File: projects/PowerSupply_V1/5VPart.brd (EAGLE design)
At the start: 49.5 x 58.4 mm, 24 parts, among them IC1 LM2596T, IC2 LM2596T, X1 IN, X2 OUT

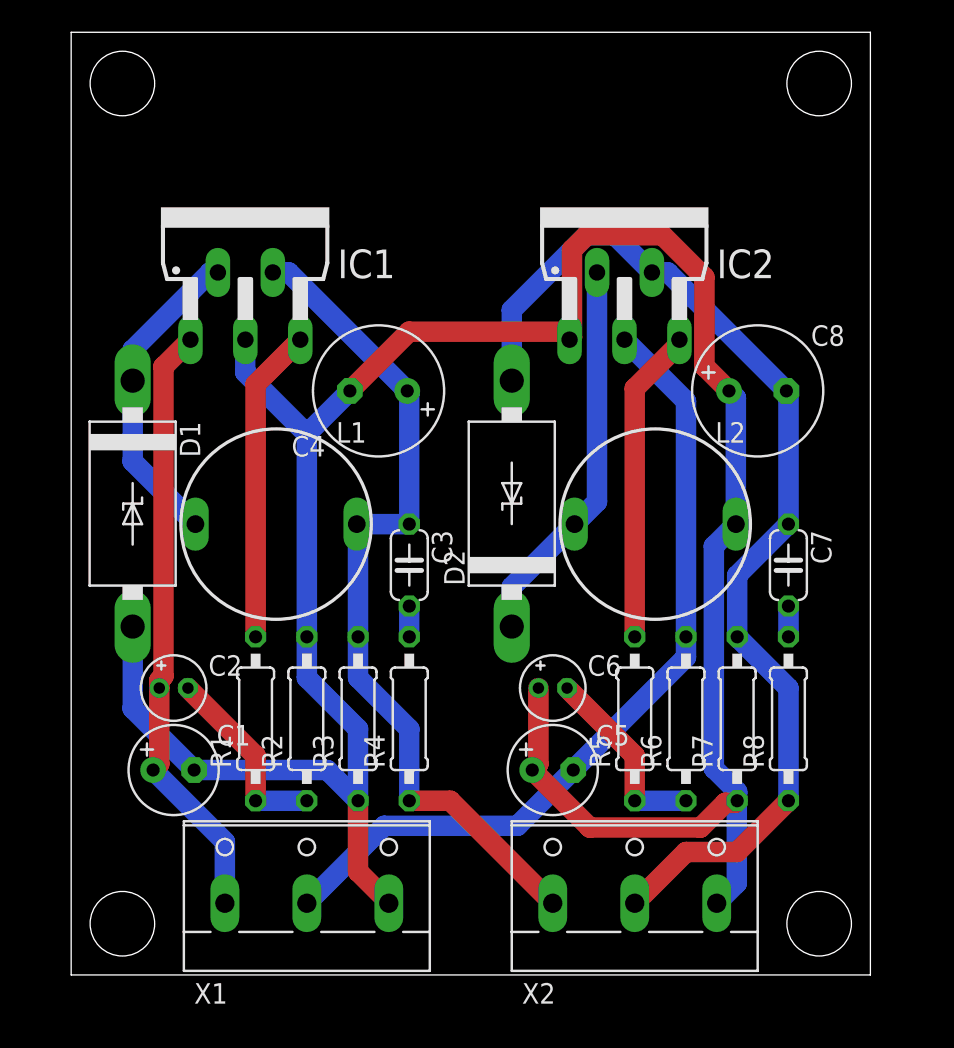
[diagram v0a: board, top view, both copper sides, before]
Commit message: refactor(5v): schematics changed
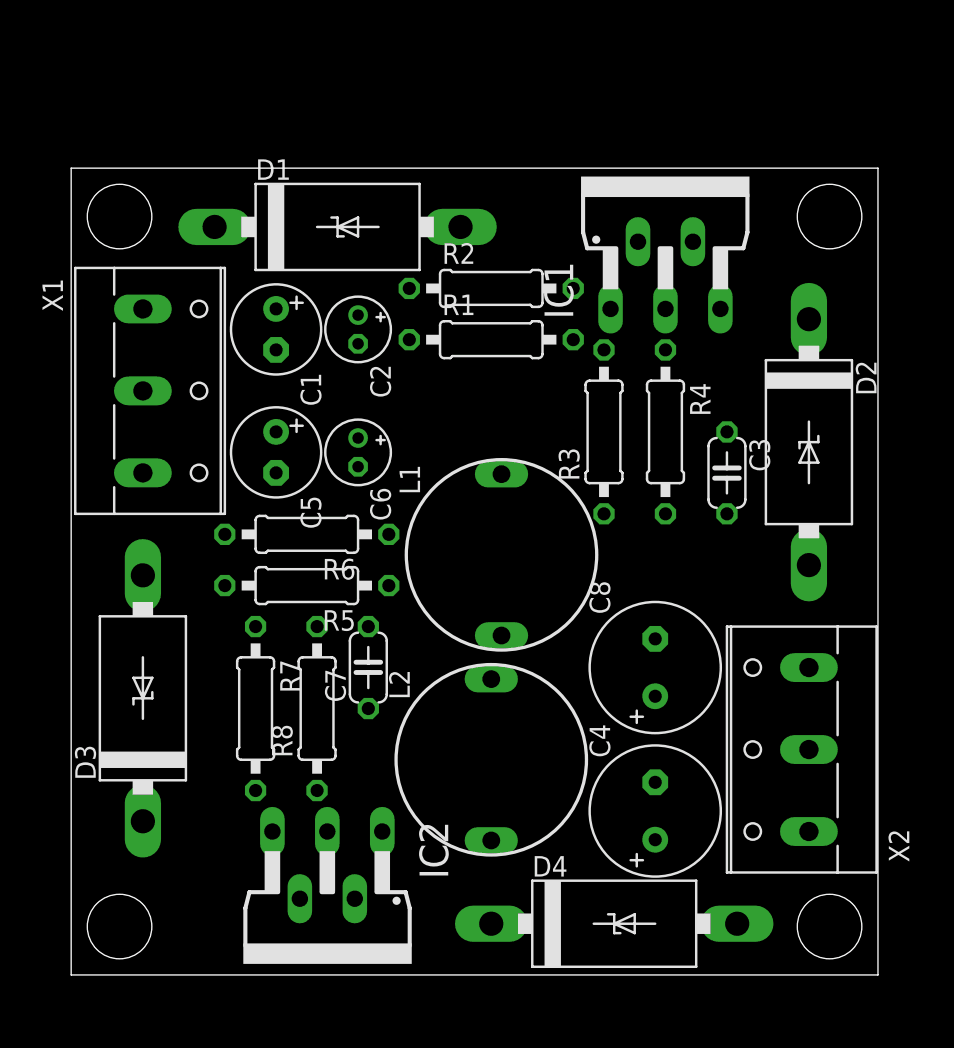
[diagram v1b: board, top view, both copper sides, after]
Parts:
- added D3, D4: 1N5822, diode:C4111-15
- moved IC2 44.6 mm to (15.9, 3.81), turned to 180 degrees
- moved X1 32.5 mm to (5.08, 36.2), turned to 270 degrees
- moved C4 31.2 mm to (36.2, 10.2), turned to 90 degrees
- moved R7 29.9 mm to (11.4, 16.5), turned to 270 degrees
- moved R8 29.2 mm to (15.2, 16.5)
- moved R2 29.0 mm to (26.0, 42.5), turned to 0 degrees
- moved C1 28.0 mm to (12.7, 40.0), turned to 270 degrees
- moved R1 27.7 mm to (26.0, 39.4), turned to 0 degrees
- moved C7 26.8 mm to (18.4, 19.1), turned to 90 degrees
- moved R6 26.1 mm to (14.6, 27.3), turned to 180 degrees
- moved C5 26.1 mm to (12.7, 32.4), turned to 270 degrees
- moved IC1 26.1 mm to (36.8, 46.4)
- moved C2 25.0 mm to (17.8, 40.0), turned to 270 degrees
- moved R4 23.8 mm to (36.8, 33.7), turned to 270 degrees
- moved R3 23.4 mm to (33.0, 33.7)
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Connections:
- net +24V: now also D1.C
- net -24V: now also D3.C, X1.3; no longer X1.2
- net -5V: now also D4.A, X2.3; no longer D2.A, X2.2
- net GND: now also D2.A, D3.A, X1.2, X2.2; no longer X1.3, X2.3
- net N$2: now also D4.C; no longer D2.C
- net N$3: now also D2.C; no longer D1.C
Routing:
- net GND: track 155.8 -> 0.00 mm
- net -5V: track 67.6 -> 0.00 mm
- net +5V: track 52.9 -> 0.00 mm
- net -24V: track 51.1 -> 0.00 mm
- net +24V: track 37.7 -> 0.00 mm
- net N$2: track 24.1 -> 0.00 mm
- net N$3: track 19.7 -> 0.00 mm
- net N$7: track 19.6 -> 0.00 mm
- net N$4: track 19.6 -> 0.00 mm
- net N$8: track 11.9 -> 0.00 mm
- net N$6: track 11.9 -> 0.00 mm
- net N$5: track 1.91 -> 0.00 mm
- net N$1: track 1.91 -> 0.00 mm
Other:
- board size 49.5 x 58.4 mm -> 50 x 50 mm

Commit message: refactor(5v): routing changed
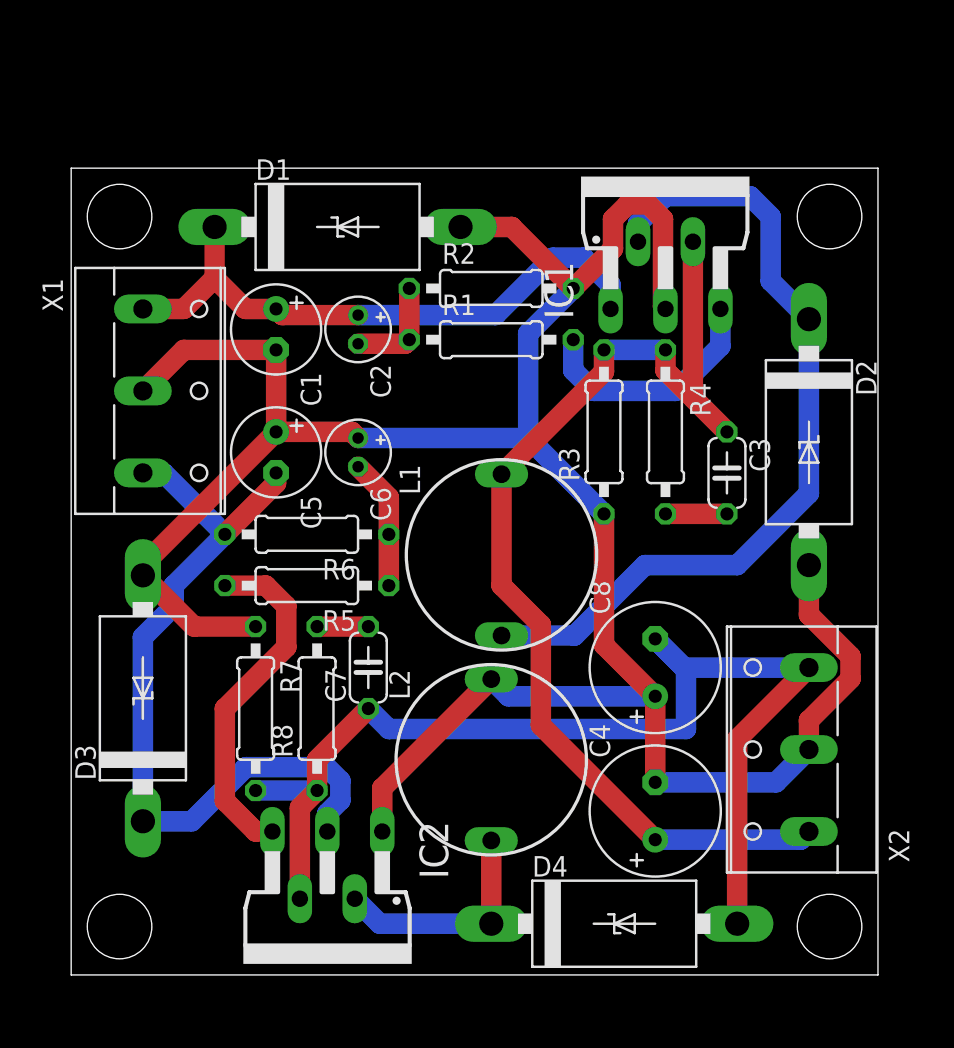
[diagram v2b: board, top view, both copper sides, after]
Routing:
- net GND: track 0.00 -> 155.9 mm
- net -5V: track 0.00 -> 71.9 mm
- net +5V: track 0.00 -> 69.8 mm
- net N$3: track 0.00 -> 51.4 mm
- net -24V: track 0.00 -> 49.1 mm
- net +24V: track 0.00 -> 38.2 mm
- net N$7: track 0.00 -> 21.7 mm
- net N$4: track 0.00 -> 15.0 mm
- net N$2: track 0.00 -> 14.3 mm
- net N$8: track 0.00 -> 8.16 mm
- net N$6: track 0.00 -> 6.46 mm
- net N$1: track 0.00 -> 3.81 mm
- net N$5: track 0.00 -> 3.17 mm

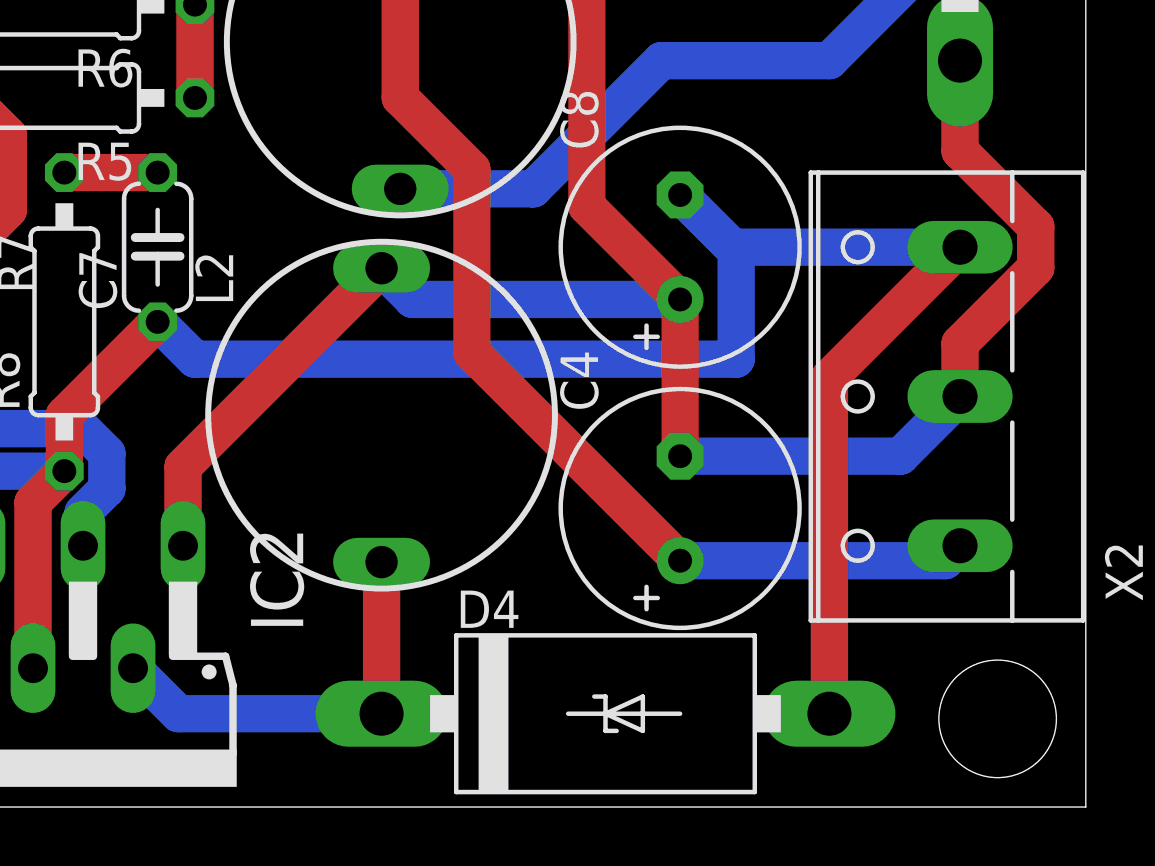
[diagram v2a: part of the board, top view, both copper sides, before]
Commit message: refactor(all): schematics and routing changed
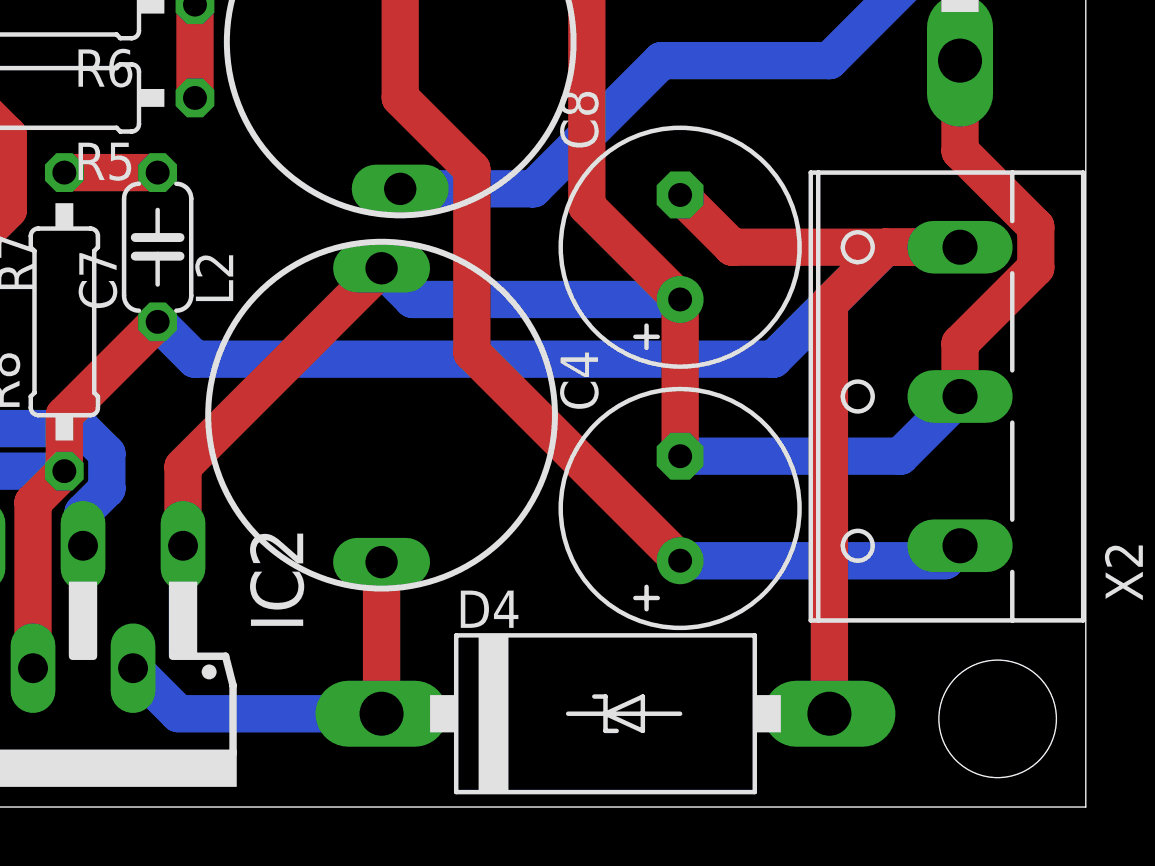
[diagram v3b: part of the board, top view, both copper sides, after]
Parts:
- C4: value 470µF -> 220µF
- C8: value 470µF -> 330µF
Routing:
- net -5V: track 71.9 -> 76.2 mm
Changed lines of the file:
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@@
 <attribute name="VALUE" x="37.973" y="33.274" size="1.27" layer="27" ratio="10" rot="R270"/>
 </element>
-<element name="C4" library="rcl" library_urn="urn:adsk.eagle:library:334" package="E3,5-8" package3d_urn="urn:adsk.eagle:package:23360/2" value="470µF" x="36.195" y="10.16" smashed="yes" rot="R90">
+<element name="C4" library="rcl" library_urn="urn:adsk.eagle:library:334" package="E3,5-8" package3d_urn="urn:adsk.eagle:package:23360/2" value="220µF" x="36.195" y="10.16" smashed="yes" rot="R90">
 <attribute name="NAME" x="33.401" y="13.462" size="1.27" layer="25" ratio="10" rot="R90"/>
 <attribute name="POPULARITY" value="13" x="66.675" y="29.21" size="1.778" layer="27" rot="R90" display="off"/>
@@
 <attribute name="VALUE" x="21.082" y="16.891" size="1.27" layer="27" ratio="10" rot="R90"/>
 </element>
-<element name="C8" library="rcl" library_urn="urn:adsk.eagle:library:334" package="E3,5-8" package3d_urn="urn:adsk.eagle:package:23360/2" value="470µF" x="36.195" y="19.05" smashed="yes" rot="R90">
+<element name="C8" library="rcl" library_urn="urn:adsk.eagle:library:334" package="E3,5-8" package3d_urn="urn:adsk.eagle:package:23360/2" value="330µF" x="36.195" y="19.05" smashed="yes" rot="R90">
 <attribute name="NAME" x="33.401" y="22.352" size="1.27" layer="25" ratio="10" rot="R90"/>
 <attribute name="POPULARITY" value="13" x="66.675" y="49.53" size="1.778" layer="27" rot="R90" display="off"/>
@@
 <wire x1="29.1074" y1="15.4696" x2="36.195" y2="8.382" width="1.27" layer="1"/>
 <wire x1="29.1074" y1="21.70288125" x2="29.1074" y2="15.4696" width="1.27" layer="1"/>
+<wire x1="33.02" y1="38.735" x2="36.83" y2="38.735" width="1.27" layer="16"/>
 <wire x1="36.195" y1="8.382" x2="45.212" y2="8.382" width="1.27" layer="16"/>
 <wire x1="45.212" y1="8.382" x2="45.72" y2="8.89" width="1.27" layer="16"/>
-<wire x1="33.02" y1="38.735" x2="36.83" y2="38.735" width="1.27" layer="16"/>
 </signal>
 <signal name="-5V">
+<contactref element="X2" pad="3"/>
 <contactref element="C8" pad="-"/>
 <contactref element="IC2" pad="4"/>
@@
 <contactref element="C7" pad="1"/>
 <contactref element="D4" pad="A"/>
-<contactref element="X2" pad="3"/>
 <wire x1="14.1732" y1="4.7244" x2="14.1732" y2="10.3632" width="1.27" layer="1"/>
 <wire x1="14.1732" y1="10.3632" x2="15.24" y2="11.43" width="1.27" layer="1"/>
 <wire x1="15.24" y1="11.43" x2="15.24" y2="13.335" width="1.27" layer="1"/>
 <wire x1="15.24" y1="13.335" x2="18.415" y2="16.51" width="1.27" layer="1"/>
-<wire x1="41.275" y1="3.175" x2="41.275" y2="14.605" width="1.27" layer="1"/>
-<wire x1="41.275" y1="14.605" x2="45.72" y2="19.05" width="1.27" layer="1"/>
 <wire x1="11.43" y1="11.43" x2="15.24" y2="11.43" width="1.27" layer="16"/>
-<wire x1="45.72" y1="19.05" x2="37.973" y2="19.05" width="1.27" layer="16"/>
-<wire x1="37.973" y1="19.05" x2="36.195" y2="20.828" width="1.27" layer="16"/>
 <wire x1="18.415" y1="16.51" x2="19.685" y2="15.24" width="1.27" layer="16"/>
-<wire x1="19.685" y1="15.24" x2="38.1" y2="15.24" width="1.27" layer="16"/>
-<wire x1="38.1" y1="15.24" x2="38.1" y2="18.923" width="1.27" layer="16"/>
-<wire x1="38.1" y1="18.923" x2="36.195" y2="20.828" width="1.27" layer="16"/>
+<wire x1="41.275" y1="3.175" x2="41.275" y2="17.145" width="1.27" layer="1"/>
+<wire x1="41.275" y1="17.145" x2="43.18" y2="19.05" width="1.27" layer="1"/>
+<wire x1="43.18" y1="19.05" x2="45.72" y2="19.05" width="1.27" layer="1"/>
+<wire x1="45.72" y1="19.05" x2="37.973" y2="19.05" width="1.27" layer="1"/>
+<wire x1="37.973" y1="19.05" x2="36.195" y2="20.828" width="1.27" layer="1"/>
+<wire x1="39.37" y1="15.24" x2="43.18" y2="19.05" width="1.27" layer="16"/>
+<wire x1="43.18" y1="19.05" x2="45.72" y2="19.05" width="1.27" layer="16"/>
+<wire x1="19.685" y1="15.24" x2="39.37" y2="15.24" width="1.27" layer="16"/>
 </signal>
 </signals>
